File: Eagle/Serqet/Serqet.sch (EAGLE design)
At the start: 61 parts

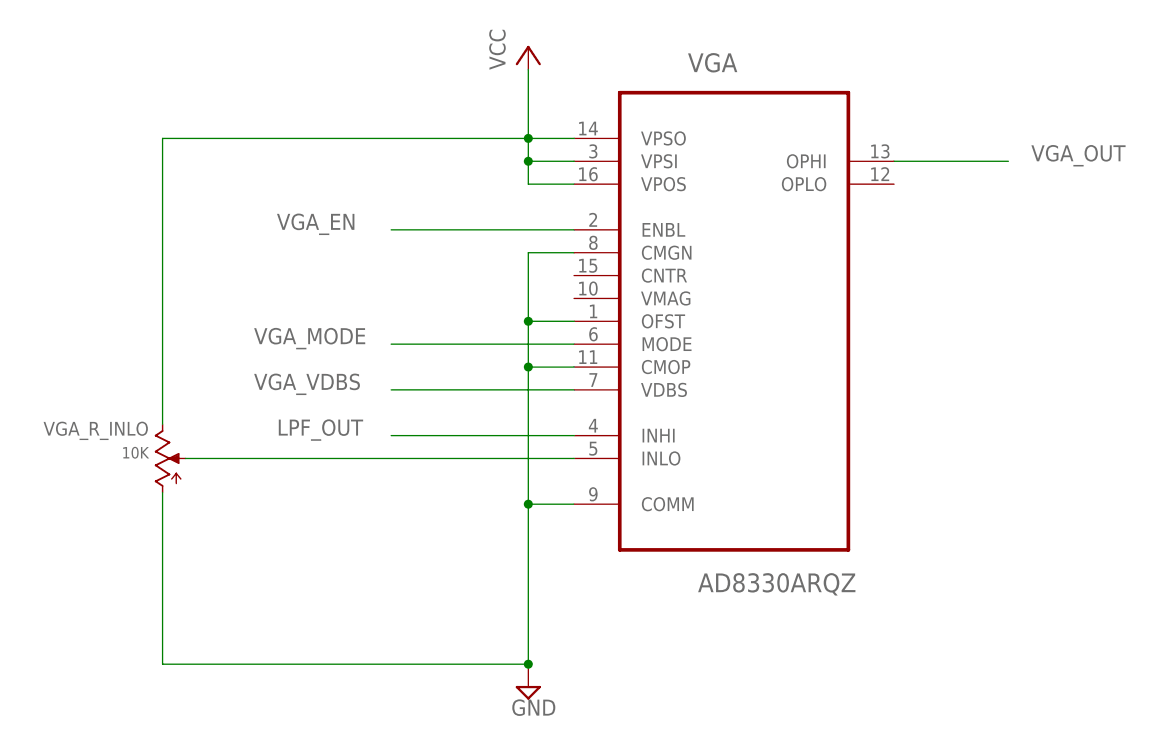
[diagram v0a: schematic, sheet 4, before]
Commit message: Fixed LPF and VGA enables
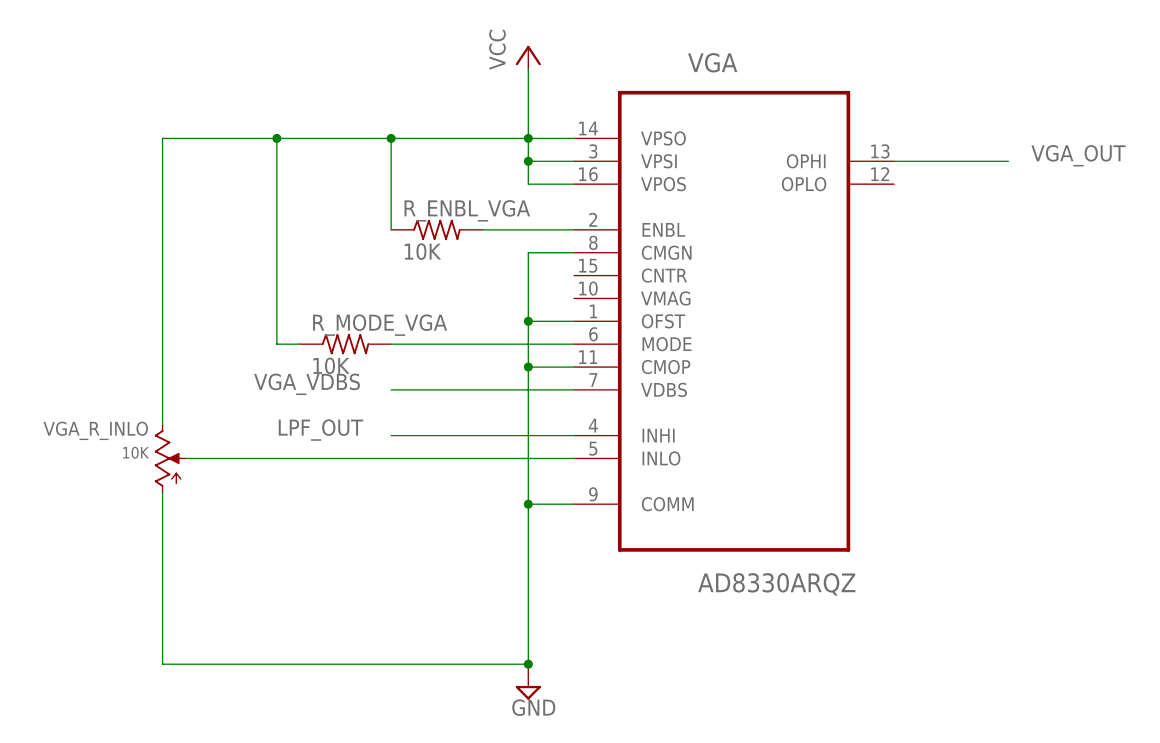
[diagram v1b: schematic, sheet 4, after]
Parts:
- added R_ENBL_VGA, R_EN_LPF, R_MODE_VGA: 10K, rcl:R-US_R0603
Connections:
- removed net VGA_EN: VGA.ENBL
- new net N$27: R_ENBL_VGA.2, VGA.ENBL
- new net N$28: OP_AMP_LPF.ENABLE, R_EN_LPF.1
- net VCC: now also R_ENBL_VGA.1, R_EN_LPF.2, R_MODE_VGA.1
- net VGA_MODE: now also R_MODE_VGA.2
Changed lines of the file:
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@@
 <part name="VGA_TO_ADC" library="resistor" deviceset="R-US_" device="R0603" value="0K"/>
 <part name="BYPASS_ATTEN_MICRO" library="resistor" deviceset="R-US_" device="R0603" value="0K"/>
+<part name="R_ENBL_VGA" library="rcl" deviceset="R-US_" device="R0603" value="10K"/>
+<part name="R_EN_LPF" library="rcl" deviceset="R-US_" device="R0603" value="10K"/>
+<part name="R_MODE_VGA" library="rcl" deviceset="R-US_" device="R0603" value="10K"/>
 </parts>
 <sheets>
@@
 <instance part="SUPPLY11" gate="GND" x="22.86" y="10.16"/>
 <instance part="VGA_R_INLO" gate="G$1" x="-17.78" y="35.56"/>
+<instance part="R_ENBL_VGA" gate="G$1" x="12.7" y="60.96"/>
+<instance part="R_MODE_VGA" gate="G$1" x="2.54" y="48.26"/>
 </instances>
 <busses>
@@
 <wire x1="22.86" y1="66.04" x2="22.86" y2="68.58" width="0.1524" layer="91"/>
 <junction x="22.86" y="68.58"/>
-<wire x1="-17.78" y1="71.12" x2="22.86" y2="71.12" width="0.1524" layer="91"/>
+<wire x1="-17.78" y1="71.12" x2="-5.08" y2="71.12" width="0.1524" layer="91"/>
+<wire x1="-5.08" y1="71.12" x2="7.62" y2="71.12" width="0.1524" layer="91"/>
+<wire x1="7.62" y1="71.12" x2="22.86" y2="71.12" width="0.1524" layer="91"/>
 <wire x1="-17.78" y1="39.37" x2="-17.78" y2="71.12" width="0.1524" layer="91"/>
 <pinref part="VGA_R_INLO" gate="G$1" pin="CW"/>
-</segment>
-</net>
-<net name="VGA_EN" class="0">
-<segment>
-<pinref part="VGA" gate="A" pin="ENBL"/>
-<wire x1="27.94" y1="60.96" x2="7.62" y2="60.96" width="0.1524" layer="91"/>
-<label x="-5.08" y="60.96" size="1.778" layer="95"/>
+<pinref part="R_ENBL_VGA" gate="G$1" pin="1"/>
+<wire x1="7.62" y1="60.96" x2="7.62" y2="71.12" width="0.1524" layer="91"/>
+<junction x="7.62" y="71.12"/>
+<pinref part="R_MODE_VGA" gate="G$1" pin="1"/>
+<wire x1="-2.54" y1="48.26" x2="-5.08" y2="48.26" width="0.1524" layer="91"/>
+<wire x1="-5.08" y1="48.26" x2="-5.08" y2="71.12" width="0.1524" layer="91"/>
+<junction x="-5.08" y="71.12"/>
 </segment>
 </net>
@@
 <pinref part="VGA" gate="A" pin="MODE"/>
 <wire x1="27.94" y1="48.26" x2="7.62" y2="48.26" width="0.1524" layer="91"/>
-<label x="-7.62" y="48.26" size="1.778" layer="95"/>
+<pinref part="R_MODE_VGA" gate="G$1" pin="2"/>
 </segment>
 </net>
@@
 </segment>
 </net>
+<net name="N$27" class="0">
+<segment>
+<pinref part="VGA" gate="A" pin="ENBL"/>
+<pinref part="R_ENBL_VGA" gate="G$1" pin="2"/>
+<wire x1="27.94" y1="60.96" x2="17.78" y2="60.96" width="0.1524" layer="91"/>
+</segment>
+</net>
 </nets>
 </sheet>
@@
 <instance part="OP_AMP_LPF" gate="G$1" x="45.72" y="50.8"/>
 <instance part="SUPPLY10" gate="GND" x="10.16" y="17.78"/>
-<instance part="P+4" gate="VCC" x="40.64" y="71.12"/>
+<instance part="P+4" gate="VCC" x="40.64" y="78.74"/>
 <instance part="R1_LPF" gate="G$1" x="-15.24" y="48.26"/>
 <instance part="R2_LPF" gate="G$1" x="-2.54" y="48.26"/>
@@
 <instance part="C2_LPF" gate="G$1" x="2.54" y="35.56"/>
 <instance part="C1_LPF" gate="G$1" x="17.78" y="66.04" rot="R90"/>
+<instance part="R_EN_LPF" gate="G$1" x="58.42" y="43.18"/>
 </instances>
 <busses>
@@
 <wire x1="48.26" y1="35.56" x2="48.26" y2="50.8" width="0.1524" layer="91"/>
 <junction x="48.26" y="50.8"/>
-<wire x1="48.26" y1="50.8" x2="63.5" y2="50.8" width="0.1524" layer="91"/>
+<wire x1="48.26" y1="50.8" x2="68.58" y2="50.8" width="0.1524" layer="91"/>
 <label x="63.5" y="50.8" size="1.778" layer="95"/>
 <pinref part="C1_LPF" gate="G$1" pin="2"/>
@@
 <net name="VCC" class="0">
 <segment>
+<pinref part="P+4" gate="VCC" pin="VCC"/>
 <pinref part="OP_AMP_LPF" gate="G$1" pin="VCC"/>
-<pinref part="P+4" gate="VCC" pin="VCC"/>
 <wire x1="40.64" y1="55.88" x2="40.64" y2="68.58" width="0.1524" layer="91"/>
-</segment>
-</net>
+<pinref part="R_EN_LPF" gate="G$1" pin="2"/>
+<wire x1="40.64" y1="68.58" x2="40.64" y2="76.2" width="0.1524" layer="91"/>
+<wire x1="63.5" y1="43.18" x2="63.5" y2="68.58" width="0.1524" layer="91"/>
+<wire x1="63.5" y1="68.58" x2="40.64" y2="68.58" width="0.1524" layer="91"/>
+<junction x="40.64" y="68.58"/>
+</segment>
+</net>
+<net name="N$28" class="0">
+<segment>
+<pinref part="OP_AMP_LPF" gate="G$1" pin="ENABLE"/>
+<wire x1="45.72" y1="45.72" x2="45.72" y2="43.18" width="0.1524" layer="91"/>
+<pinref part="R_EN_LPF" gate="G$1" pin="1"/>
+<wire x1="45.72" y1="43.18" x2="53.34" y2="43.18" width="0.1524" layer="91"/>
+</segment>
+</net>

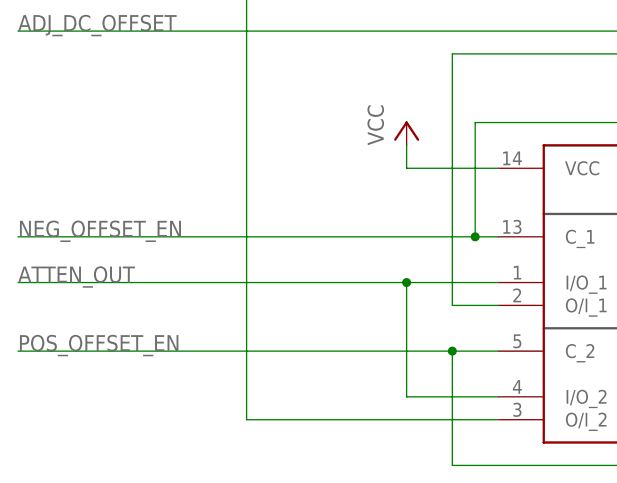
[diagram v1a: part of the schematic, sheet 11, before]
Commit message: Fixed signal conditioning bypass
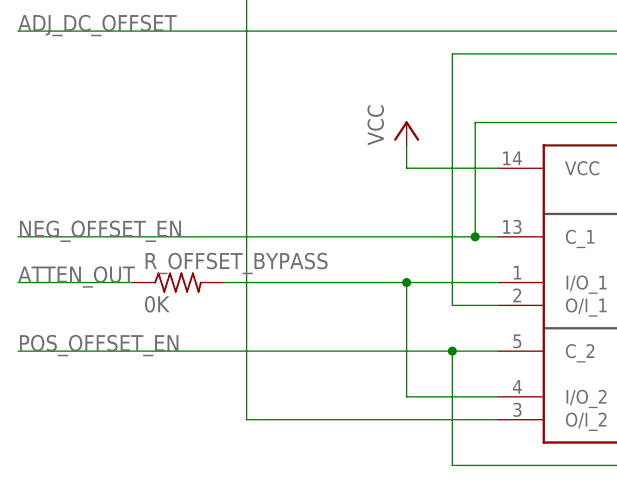
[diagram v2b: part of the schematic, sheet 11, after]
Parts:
- added R_OFFSET_BYPASS: 0K, rcl:R-US_R0603
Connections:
- new net NET_IO_1: BILATERAL_DCOFF.I/O_1, BILATERAL_DCOFF.I/O_2, R_OFFSET_BYPASS.2
- net ATTEN_OUT: now also R_OFFSET_BYPASS.1; no longer BILATERAL_DCOFF.I/O_1, BILATERAL_DCOFF.I/O_2
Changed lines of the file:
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@@
 <part name="R_EN_LPF" library="rcl" deviceset="R-US_" device="R0603" value="10K"/>
 <part name="R_MODE_VGA" library="rcl" deviceset="R-US_" device="R0603" value="10K"/>
+<part name="R_OFFSET_BYPASS" library="rcl" deviceset="R-US_" device="R0603" value="0K"/>
 </parts>
 <sheets>
@@
 <instance part="SUPPLY15" gate="GND" x="35.56" y="7.62"/>
 <instance part="P+3" gate="VCC" x="-12.7" y="15.24"/>
+<instance part="R_OFFSET_BYPASS" gate="G$1" x="-38.1" y="-2.54"/>
 </instances>
 <busses>
@@
 <net name="ATTEN_OUT" class="0">
 <segment>
-<pinref part="BILATERAL_DCOFF" gate="G$1" pin="I/O_1"/>
-<wire x1="-2.54" y1="-2.54" x2="-12.7" y2="-2.54" width="0.1524" layer="91"/>
+<pinref part="R_OFFSET_BYPASS" gate="G$1" pin="1"/>
+<wire x1="-43.18" y1="-2.54" x2="-55.88" y2="-2.54" width="0.1524" layer="91"/>
 <label x="-55.88" y="-2.54" size="1.778" layer="95"/>
-<wire x1="-12.7" y1="-2.54" x2="-12.7" y2="-15.24" width="0.1524" layer="91"/>
-<junction x="-12.7" y="-2.54"/>
-<pinref part="BILATERAL_DCOFF" gate="G$1" pin="I/O_2"/>
-<wire x1="-12.7" y1="-15.24" x2="-2.54" y2="-15.24" width="0.1524" layer="91"/>
-<wire x1="-12.7" y1="-2.54" x2="-55.88" y2="-2.54" width="0.1524" layer="91"/>
 </segment>
 </net>
@@
 </segment>
 </net>
+<net name="NET_IO_1" class="0">
+<segment>
+<pinref part="BILATERAL_DCOFF" gate="G$1" pin="I/O_1"/>
+<wire x1="-2.54" y1="-2.54" x2="-12.7" y2="-2.54" width="0.1524" layer="91"/>
+<wire x1="-12.7" y1="-2.54" x2="-12.7" y2="-15.24" width="0.1524" layer="91"/>
+<pinref part="BILATERAL_DCOFF" gate="G$1" pin="I/O_2"/>
+<wire x1="-12.7" y1="-15.24" x2="-2.54" y2="-15.24" width="0.1524" layer="91"/>
+<pinref part="R_OFFSET_BYPASS" gate="G$1" pin="2"/>
+<wire x1="-12.7" y1="-2.54" x2="-33.02" y2="-2.54" width="0.1524" layer="91"/>
+<junction x="-12.7" y="-2.54"/>
+</segment>
+</net>

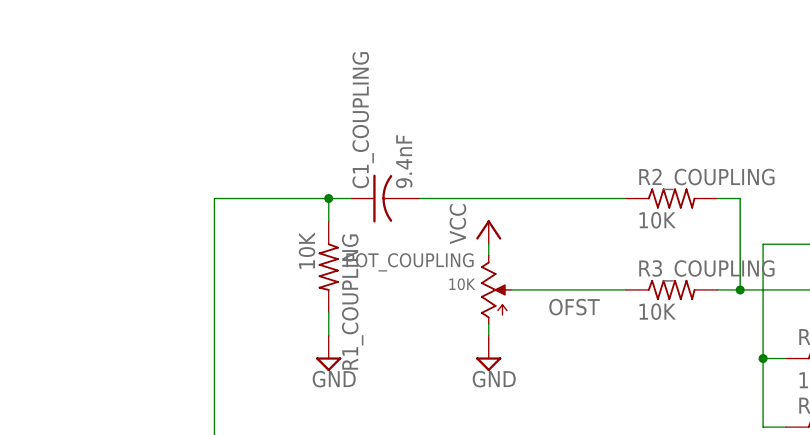
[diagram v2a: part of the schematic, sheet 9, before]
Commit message: Changed coupling capacitor value to one that exists on DigiKey
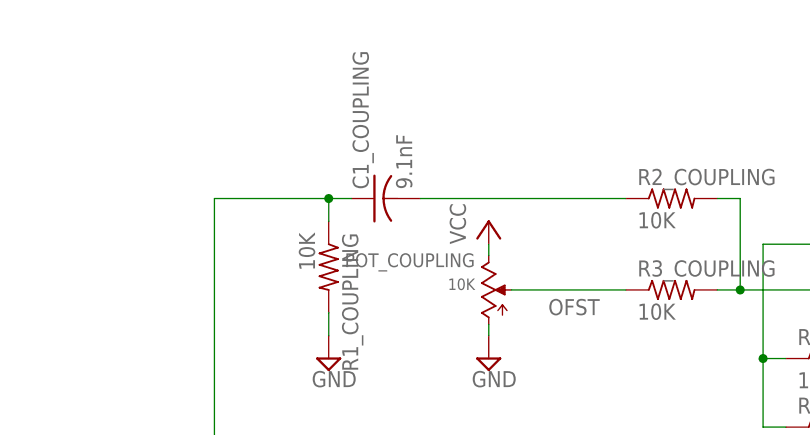
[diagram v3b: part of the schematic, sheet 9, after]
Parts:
- C1_COUPLING: value 9.4nF -> 9.1nF
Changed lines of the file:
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@@
 <part name="POT_COUPLING" library="QuantumOptics" deviceset="POT" device="-CHEAP_3HOLE_TRIM" value="10K"/>
 <part name="R1_COUPLING" library="rcl" deviceset="R-US_" device="R0603" value="10K"/>
-<part name="C1_COUPLING" library="rcl" deviceset="C-US" device="C0603" value="9.4nF"/>
+<part name="C1_COUPLING" library="rcl" deviceset="C-US" device="C0603" value="9.1nF"/>
 <part name="BILATERAL_COUPLING" library="SparkFun-DigitalIC" deviceset="TC74HC4066AFT" device=""/>
 <part name="BILATERAL_DCOFF" library="SparkFun-DigitalIC" deviceset="TC74HC4066AFT" device=""/>

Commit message: Inverted bit order between ADC and FPGA for better layout
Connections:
- net ADC_OUT_0: now also FPGA.ADC_OUT_7; no longer FPGA.ADC_OUT_0
- net ADC_OUT_1: now also FPGA.ADC_OUT_6; no longer FPGA.ADC_OUT_1
- net ADC_OUT_2: now also FPGA.ADC_OUT_5; no longer FPGA.ADC_OUT_2
- net ADC_OUT_3: now also FPGA.ADC_OUT_4; no longer FPGA.ADC_OUT_3
- net ADC_OUT_4: now also FPGA.ADC_OUT_3; no longer FPGA.ADC_OUT_4
- net ADC_OUT_5: now also FPGA.ADC_OUT_2; no longer FPGA.ADC_OUT_5
- net ADC_OUT_6: now also FPGA.ADC_OUT_1; no longer FPGA.ADC_OUT_6
- net ADC_OUT_7: now also FPGA.ADC_OUT_0; no longer FPGA.ADC_OUT_7
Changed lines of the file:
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@@
 </busses>
 <nets>
-<net name="ADC_OUT_0" class="0">
-<segment>
-<pinref part="FPGA" gate="G$1" pin="ADC_OUT_0"/>
-<wire x1="22.86" y1="86.36" x2="10.16" y2="86.36" width="0.1524" layer="91"/>
-</segment>
-</net>
-<net name="ADC_OUT_1" class="0">
-<segment>
-<pinref part="FPGA" gate="G$1" pin="ADC_OUT_1"/>
-<wire x1="22.86" y1="83.82" x2="10.16" y2="83.82" width="0.1524" layer="91"/>
-</segment>
-</net>
-<net name="ADC_OUT_2" class="0">
-<segment>
-<pinref part="FPGA" gate="G$1" pin="ADC_OUT_2"/>
-<wire x1="22.86" y1="81.28" x2="10.16" y2="81.28" width="0.1524" layer="91"/>
-</segment>
-</net>
-<net name="ADC_OUT_4" class="0">
-<segment>
-<pinref part="FPGA" gate="G$1" pin="ADC_OUT_4"/>
-<wire x1="22.86" y1="76.2" x2="10.16" y2="76.2" width="0.1524" layer="91"/>
-</segment>
-</net>
-<net name="ADC_OUT_5" class="0">
-<segment>
-<pinref part="FPGA" gate="G$1" pin="ADC_OUT_5"/>
-<wire x1="22.86" y1="73.66" x2="10.16" y2="73.66" width="0.1524" layer="91"/>
-</segment>
-</net>
-<net name="ADC_OUT_6" class="0">
-<segment>
-<pinref part="FPGA" gate="G$1" pin="ADC_OUT_6"/>
-<wire x1="22.86" y1="71.12" x2="10.16" y2="71.12" width="0.1524" layer="91"/>
-</segment>
-</net>
-<net name="ADC_OUT_7" class="0">
-<segment>
-<pinref part="FPGA" gate="G$1" pin="ADC_OUT_7"/>
-<wire x1="22.86" y1="68.58" x2="10.16" y2="68.58" width="0.1524" layer="91"/>
-</segment>
-</net>
-<net name="ADC_OUT_3" class="0">
-<segment>
-<pinref part="FPGA" gate="G$1" pin="ADC_OUT_3"/>
-<wire x1="22.86" y1="78.74" x2="10.16" y2="78.74" width="0.1524" layer="91"/>
-</segment>
-</net>
 <net name="ADC_ENCODE" class="0">
 <segment>
@@
 </segment>
 </net>
+<net name="ADC_OUT_7" class="0">
+<segment>
+<pinref part="FPGA" gate="G$1" pin="ADC_OUT_0"/>
+<wire x1="22.86" y1="86.36" x2="10.16" y2="86.36" width="0.1524" layer="91"/>
+</segment>
+</net>
+<net name="ADC_OUT_6" class="0">
+<segment>
+<pinref part="FPGA" gate="G$1" pin="ADC_OUT_1"/>
+<wire x1="22.86" y1="83.82" x2="10.16" y2="83.82" width="0.1524" layer="91"/>
+</segment>
+</net>
+<net name="ADC_OUT_5" class="0">
+<segment>
+<pinref part="FPGA" gate="G$1" pin="ADC_OUT_2"/>
+<wire x1="22.86" y1="81.28" x2="10.16" y2="81.28" width="0.1524" layer="91"/>
+</segment>
+</net>
+<net name="ADC_OUT_4" class="0">
+<segment>
+<pinref part="FPGA" gate="G$1" pin="ADC_OUT_3"/>
+<wire x1="22.86" y1="78.74" x2="10.16" y2="78.74" width="0.1524" layer="91"/>
+</segment>
+</net>
+<net name="ADC_OUT_3" class="0">
+<segment>
+<pinref part="FPGA" gate="G$1" pin="ADC_OUT_4"/>
+<wire x1="22.86" y1="76.2" x2="10.16" y2="76.2" width="0.1524" layer="91"/>
+</segment>
+</net>
+<net name="ADC_OUT_2" class="0">
+<segment>
+<pinref part="FPGA" gate="G$1" pin="ADC_OUT_5"/>
+<wire x1="22.86" y1="73.66" x2="10.16" y2="73.66" width="0.1524" layer="91"/>
+</segment>
+</net>
+<net name="ADC_OUT_1" class="0">
+<segment>
+<pinref part="FPGA" gate="G$1" pin="ADC_OUT_6"/>
+<wire x1="22.86" y1="71.12" x2="10.16" y2="71.12" width="0.1524" layer="91"/>
+</segment>
+</net>
+<net name="ADC_OUT_0" class="0">
+<segment>
+<pinref part="FPGA" gate="G$1" pin="ADC_OUT_7"/>
+<wire x1="22.86" y1="68.58" x2="10.16" y2="68.58" width="0.1524" layer="91"/>
+</segment>
+</net>
